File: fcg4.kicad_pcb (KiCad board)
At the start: 4 copper layers, 34 x 34 mm, 107 parts, among them IC1 MP9943AGQ-Z, IC2 MP9943AGQ-Z, J1 USB4105-GF-A-120, J2 SM08B-SRSS-TB, U1 STM32G473CEUx, U10 MAX40200ANS_T, U11 MAX40200ANS_T, U2 ICM-42688-P, U4 AP2112K-3.3TRG1, U5 AP2112K-1.8TRG1, Y1 ECS-240-6-37B-7KM-TR

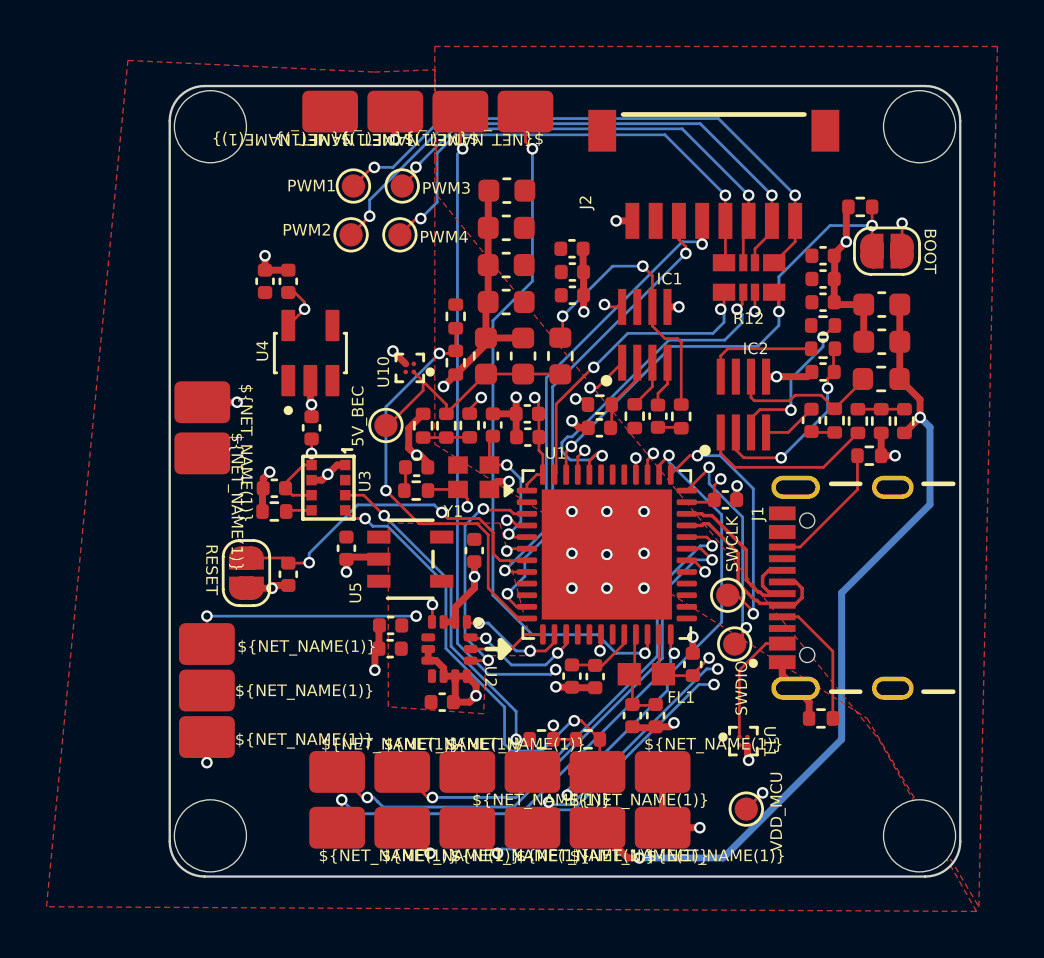
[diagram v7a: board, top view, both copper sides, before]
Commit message: Update component properties in schematics with manufacturer details and datasheets
- Added manufacturer name, part number, and LCSC part name for various components in mcu.kicad_sch, power.kicad_sch, and sensor.kicad_sch.
- Updated datasheet links for components to point to the correct URLs.
- Ensured all new properties are hidden in the schematic view.
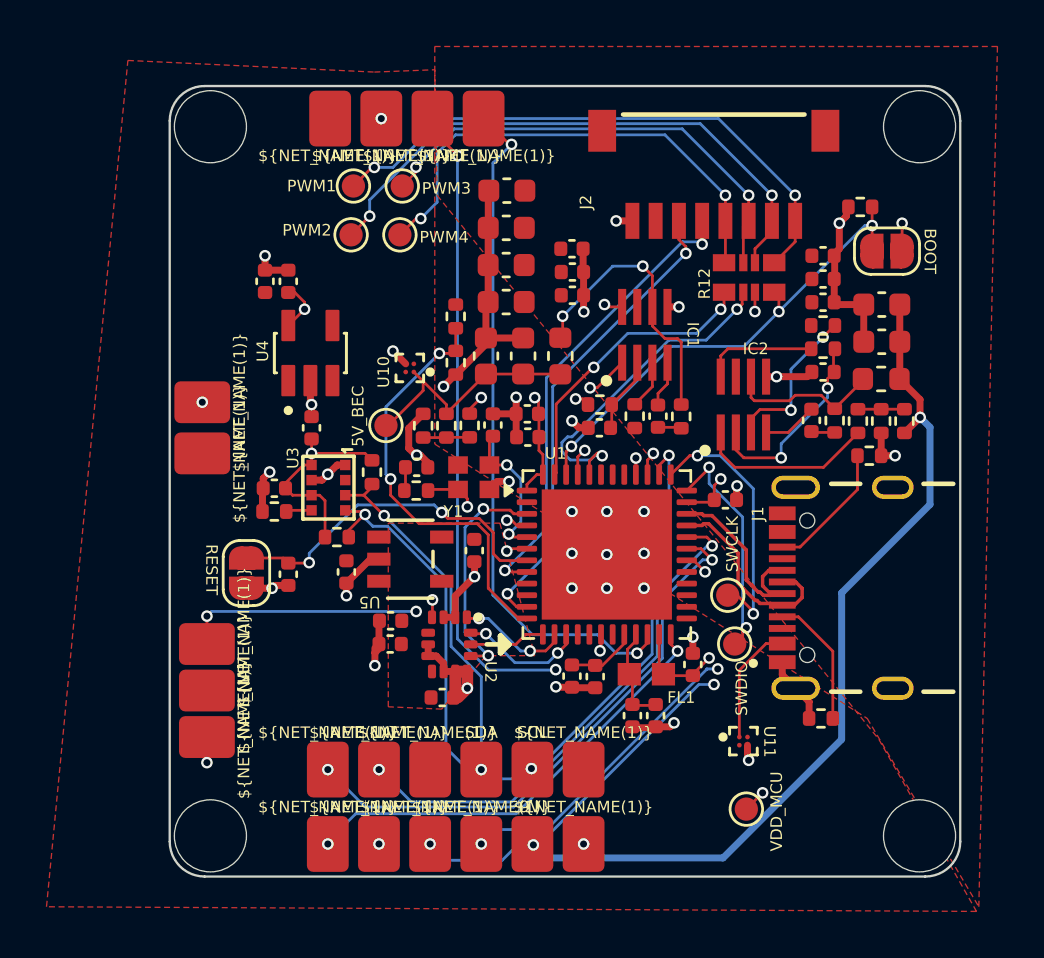
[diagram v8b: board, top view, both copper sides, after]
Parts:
- U23: value ~ -> SDA
- U26: value ~ -> SCL
- U31: value ~ -> 9V
- moved R23 13.9 mm to (7.19, 19.4)
- moved R22 13.6 mm to (8.70, 16.6), turned to 90 degrees
- moved U28 3.47 mm to (17.8, 32.6), turned to 90 degrees
- moved U9 3.40 mm to (17.8, 29.4), turned to 90 degrees
- moved U31 2.89 mm to (15.6, 32.6), turned to 90 degrees
- moved U26 2.80 mm to (15.6, 29.4), turned to 90 degrees
- moved U30 2.31 mm to (13.4, 32.6), turned to 90 degrees
- moved U23 2.20 mm to (13.4, 29.4), turned to 90 degrees
- moved U14 1.82 mm to (13.5, 1.40), turned to 90 degrees
- moved U29 1.75 mm to (11.2, 32.6), turned to 90 degrees
- moved U8 1.60 mm to (11.2, 29.4), turned to 90 degrees
- moved U15 1.24 mm to (11.3, 1.40), turned to 90 degrees
- moved U32 1.22 mm to (9.00, 32.6), turned to 90 degrees
- moved C20 1.02 mm to (7.60, 20.9)
- moved U7 1.00 mm to (9.00, 29.4), turned to 90 degrees
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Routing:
- net GND: track 74.3 -> 65.6 mm
- net I2C1_SCL: track 42.3 -> 36.8 mm, vias 4 -> 3
- net TX4: track 23.5 -> 27.3 mm
- net VDD_MCU: track 21.2 -> 24.6 mm, vias 8 -> 7
- net 9V_BEC: track 34.9 -> 37.4 mm
- net RX4: track 28.7 -> 30.2 mm
- net MOTOR1: track 22.2 -> 21.0 mm
- net RX1: track 21.3 -> 22.3 mm
- net MOTOR3: track 15.1 -> 14.4 mm
- net MOTOR4: track 13.1 -> 12.6 mm
